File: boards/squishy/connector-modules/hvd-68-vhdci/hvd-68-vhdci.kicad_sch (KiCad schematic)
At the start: 14 parts, among them J1 SCSI PHY Mezz, J3 Conn_01x04, J4 VHDCI, U1 M24C02-RMC

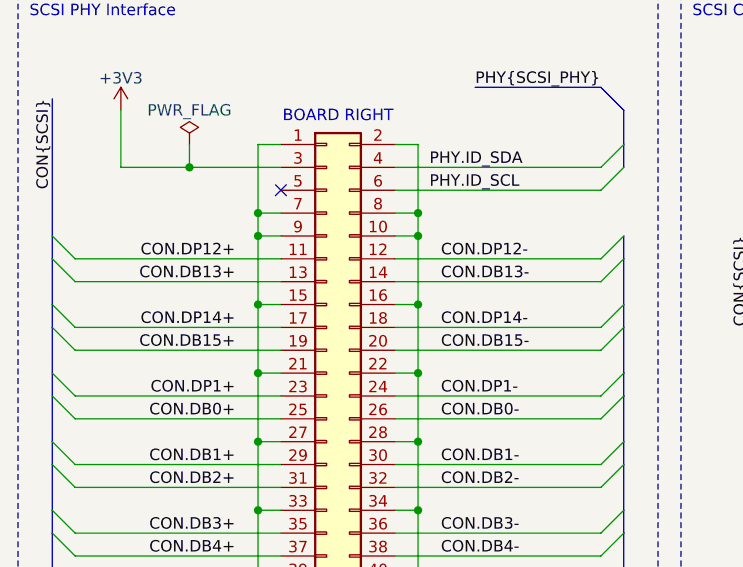
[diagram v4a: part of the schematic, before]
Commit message: squishy: connectors: s/DP12/DB12/g s/DP14/DB14/g
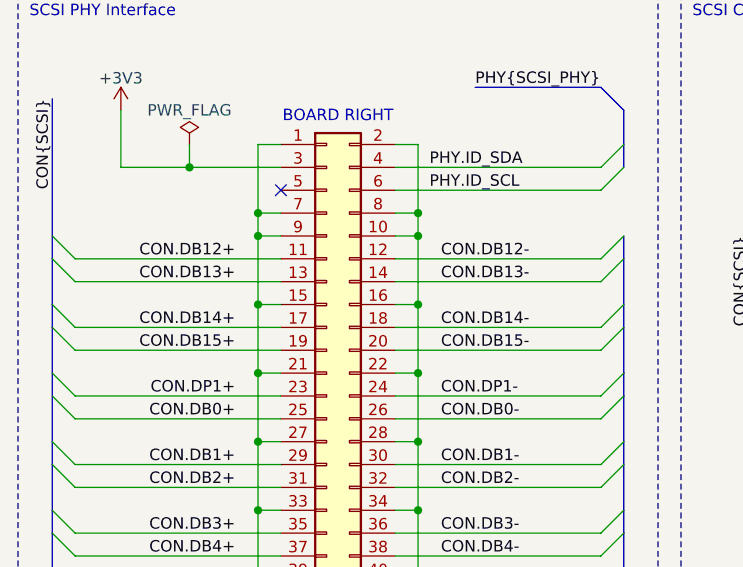
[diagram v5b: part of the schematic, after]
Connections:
- net CON.DP12+ is gone; now on net CON.DB12+: J1.11 (Pin_11)
- net CON.DP12- is gone; now on net CON.DB12-: J1.12 (Pin_12)
- net CON.DP14+ is gone; now on net CON.DB14+: J1.17 (Pin_17)
- net CON.DP14- is gone; now on net CON.DB14-: J1.18 (Pin_18)
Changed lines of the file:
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@@
 		)
 	)
-	(label "CON.DP14-"
+	(label "CON.DB14-"
 		(at 60.96 52.07 0)
 		(fields_autoplaced yes)
@@
 		)
 	)
-	(label "CON.DP12+"
+	(label "CON.DB12+"
 		(at 38.1 44.45 180)
 		(fields_autoplaced yes)
@@
 		)
 	)
-	(label "CON.DP12-"
+	(label "CON.DB12-"
 		(at 60.96 44.45 0)
 		(fields_autoplaced yes)
@@
 		)
 	)
-	(label "CON.DP14+"
+	(label "CON.DB14+"
 		(at 38.1 52.07 180)
 		(fields_autoplaced yes)

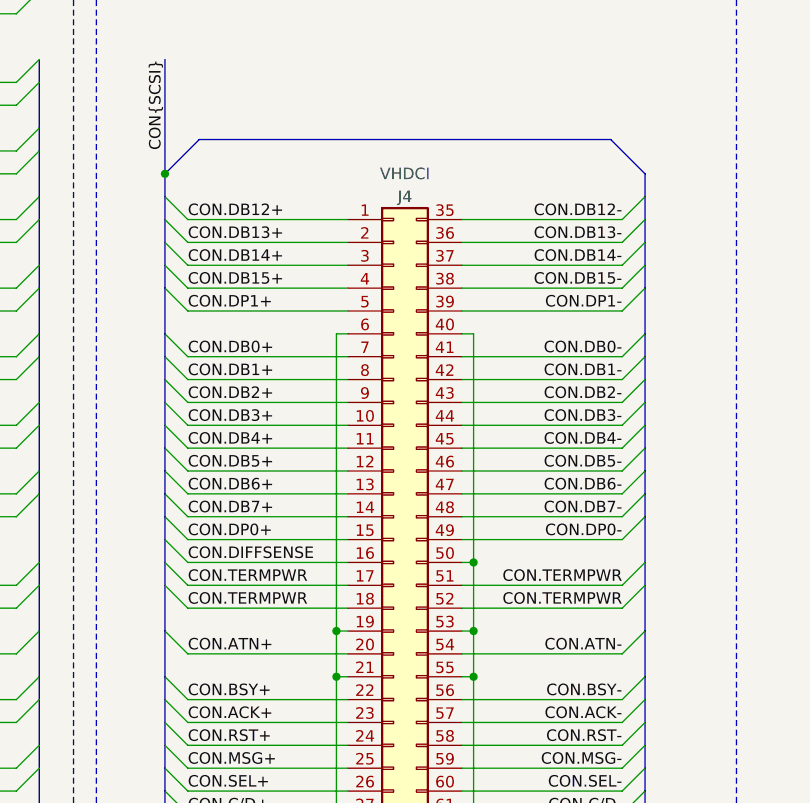
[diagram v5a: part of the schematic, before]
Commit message: squishy: connectors: updated SCSI connector metadata for hvd-68-vhdci
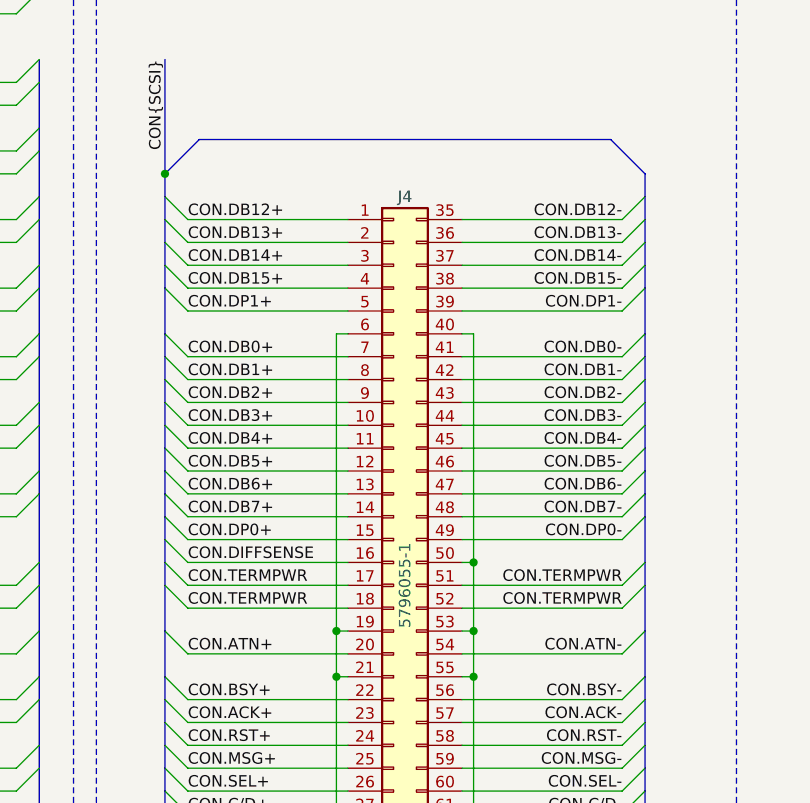
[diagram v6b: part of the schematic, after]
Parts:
- J4: value VHDCI -> 5796055-1; MFR (none) -> TE Connectivity; MPN (none) -> 5796055-1; URL (none) -> https://www.te.com/en/product-5796055-1.html
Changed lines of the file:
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@@
 			)
 		)
-		(property "Value" "VHDCI"
-			(at 121.92 54.61 0)
+		(property "Value" "5796055-1"
+			(at 121.92 100.33 90)
 			(effects
 				(font
@@
 			)
 		)
-		(property "Datasheet" "~"
+		(property "Datasheet" "https://www.te.com/commerce/DocumentDelivery/DDEController?Action=showdoc&DocId=Specification+Or+Standard%7F114-6057%7FD%7Fpdf%7FEnglish%7FENG_SS_114-6057_D.pdf%7F5796055-1"
 			(at 120.65 107.95 0)
 			(effects
@@
 			)
 		)
-		(property "Description" "Generic connector, double row, 02x34 counter clockwise pin numbering scheme (similar to DIP package numbering), with shielding"
+		(property "Description" "CHAMP 0.8mm Right Angle 68-pin VHDCI Connector"
 			(at 121.92 100.076 0)
 			(effects
 				(font
+					(size 1.27 1.27)
+				)
+				(hide yes)
+			)
+		)
+		(property "MFR" "TE Connectivity"
+			(at 121.92 100.33 0)
+			(effects
+				(font
+					(size 1.27 1.27)
+				)
+				(hide yes)
+			)
+		)
+		(property "MPN" "5796055-1"
+			(at 121.92 100.33 0)
+			(effects
+				(font
+					(size 1.27 1.27)
+				)
+				(hide yes)
+			)
+		)
+		(property "URL" "https://www.te.com/en/product-5796055-1.html"
+			(at 121.92 100.33 0)
+			(effects
+				(font

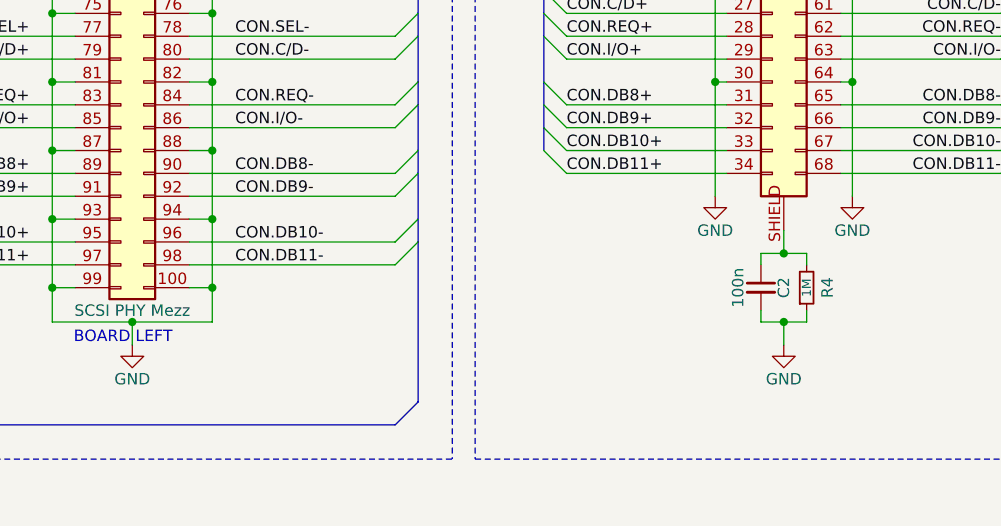
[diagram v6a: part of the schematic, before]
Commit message: squishy: connectors: cleaned up ERC on the hd-68-vhdci connector
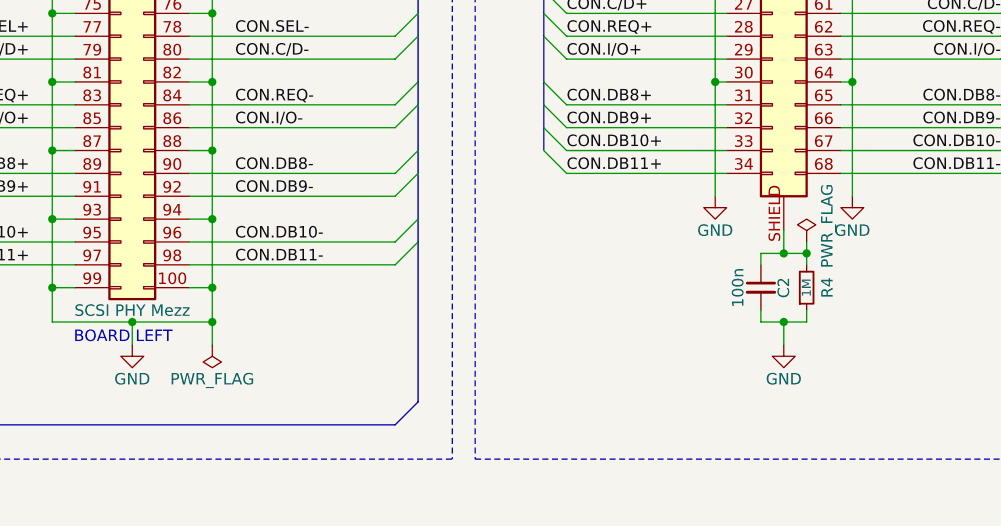
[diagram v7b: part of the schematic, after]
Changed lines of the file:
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@@
 	)
 	(junction
+		(at 124.46 152.4)
+		(diameter 0)
+		(color 0 0 0 0)
+	)
+	(junction
 		(at 58.42 125.73)
 		(diameter 0)
@@
 	)
 	(junction
+		(at 58.42 160.02)
+		(diameter 0)
+		(color 0 0 0 0)
+	)
+	(junction
 		(at 238.76 156.21)
 		(diameter 0)
@@
 	(wire
 		(pts
+			(xy 58.42 160.02) (xy 58.42 162.56)
+		)
+		(stroke
+			(width 0)
+			(type default)
+		)
+	)
+	(wire
+		(pts
 			(xy 78.74 67.31) (xy 55.88 67.31)
 		)
@@
 	(wire
 		(pts
+			(xy 124.46 151.13) (xy 124.46 152.4)
+		)
+		(stroke
+			(width 0)
+			(type default)
+		)
+	)
+	(wire
+		(pts
 			(xy 97.79 123.19) (xy 115.57 123.19)
 		)
@@
 	(symbol
 		(lib_id "power:PWR_FLAG")
+		(at 124.46 151.13 0)
+		(unit 1)
+		(exclude_from_sim no)
+		(in_bom yes)
+		(on_board yes)
+		(dnp no)
+		(property "Reference" "#FLG03"
+			(at 124.46 149.225 0)
+			(effects
+				(font
+					(size 1.27 1.27)
+				)
+				(hide yes)
+			)
+		)
+		(property "Value" "PWR_FLAG"
+			(at 126.746 149.352 90)
+			(effects
+				(font
+					(size 1.27 1.27)
+				)
+			)
+		)
+		(property "Footprint" ""
+			(at 124.46 151.13 0)
+			(effects
+				(font
+					(size 1.27 1.27)
+				)
+				(hide yes)
+			)
+		)
+		(property "Datasheet" "~"
+			(at 124.46 151.13 0)
+			(effects
+				(font
+					(size 1.27 1.27)
+				)
+				(hide yes)
+			)
+		)
+		(property "Description" "Special symbol for telling ERC where power comes from"
+			(at 124.46 151.13 0)
+			(effects
+				(font
+					(size 1.27 1.27)
+				)
+				(hide yes)
+			)
+		)
+		(pin "1"
+		)
+		(instances
+			(project "hvd-68-vhdci"
+				(path "/bd9eafec-5355-49e4-b2e3-916daacb0a86"
+					(reference "#FLG03")
+					(unit 1)
+				)
+			)
+		)
+	)
+	(symbol
+		(lib_id "power:PWR_FLAG")
 		(at 33.02 31.75 0)
 		(unit 1)
@@
 					(unit 1)
 				)
+			)
+		)
+	)
+	(symbol
+		(lib_id "power:PWR_FLAG")
+		(at 58.42 162.56 180)
+		(unit 1)
+		(exclude_from_sim no)
+		(in_bom yes)
+		(on_board yes)
+		(dnp no)
+		(property "Reference" "#FLG02"
+			(at 58.42 164.465 0)
+			(effects
+				(font
+					(size 1.27 1.27)
+				)
+				(hide yes)
+			)
+		)
+		(property "Value" "PWR_FLAG"
+			(at 58.42 166.37 0)
+			(effects
+				(font
+					(size 1.27 1.27)
+				)
+			)
+		)
+		(property "Footprint" ""
+			(at 58.42 162.56 0)
+			(effects
+				(font
+					(size 1.27 1.27)
+				)
+				(hide yes)
+			)
+		)
+		(property "Datasheet" "~"
+			(at 58.42 162.56 0)
+			(effects
+				(font
+					(size 1.27 1.27)
+				)
+				(hide yes)
+			)
+		)
+		(property "Description" "Special symbol for telling ERC where power comes from"
+			(at 58.42 162.56 0)
+			(effects
+				(font
+					(size 1.27 1.27)
+				)
+				(hide yes)
+			)
+		)
+		(pin "1"
+		)
+		(instances
+			(project "hvd-68-vhdci"
+				(path "/bd9eafec-5355-49e4-b2e3-916daacb0a86"
+					(reference "#FLG02")
+					(unit 1)
+				)

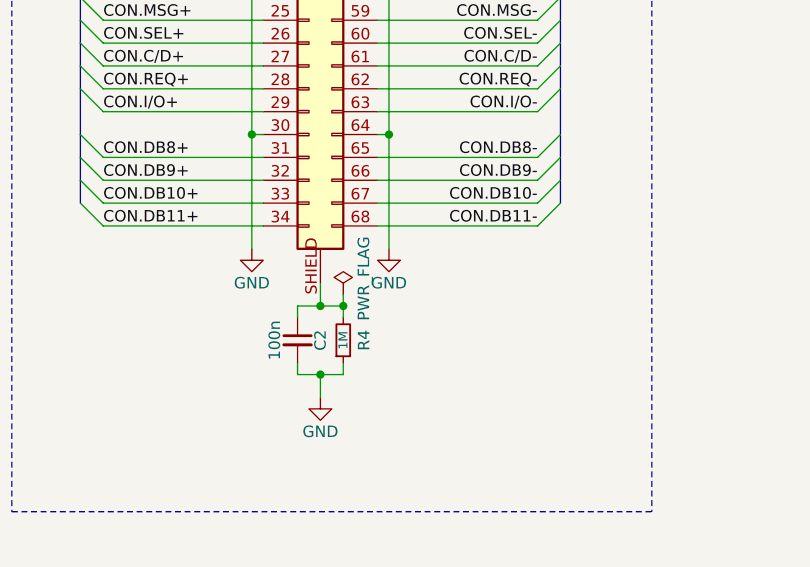
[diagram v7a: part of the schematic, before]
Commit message: squishy: connectors: Routed all and length matched half of the hvd-68-vhdci connector interface
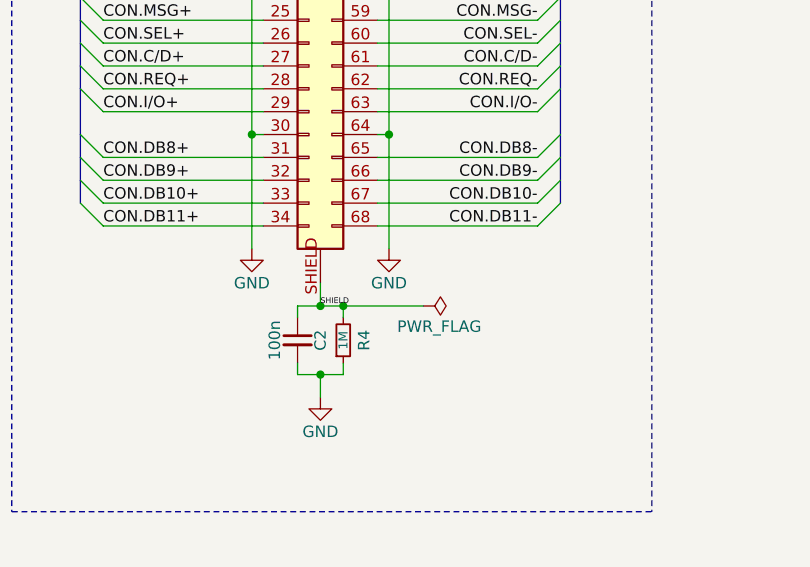
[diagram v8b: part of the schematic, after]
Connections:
- net SHIELD: now reaches C2.1, J4.SHIELD, R4.2
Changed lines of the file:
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@@
 	)
 	(junction
-		(at 124.46 152.4)
+		(at 58.42 125.73)
 		(diameter 0)
 		(color 0 0 0 0)
 	)
 	(junction
-		(at 58.42 125.73)
+		(at 40.64 64.77)
 		(diameter 0)
 		(color 0 0 0 0)
 	)
 	(junction
-		(at 40.64 64.77)
+		(at 124.46 152.4)
 		(diameter 0)
 		(color 0 0 0 0)
@@
 	(wire
 		(pts
+			(xy 124.46 152.4) (xy 133.35 152.4)
+		)
+		(stroke
+			(width 0)
+			(type default)
+		)
+	)
+	(wire
+		(pts
 			(xy 114.3 133.35) (xy 114.3 146.05)
 		)
@@
 	(wire
 		(pts
-			(xy 124.46 151.13) (xy 124.46 152.4)
-		)
-		(stroke
-			(width 0)
-			(type default)
-		)
-	)
-	(wire
-		(pts
 			(xy 97.79 123.19) (xy 115.57 123.19)
 		)
@@
 		)
 	)
+	(label "SHIELD"
+		(at 121.92 152.4 0)
+		(fields_autoplaced yes)
+		(effects
+			(font
+				(size 0.635 0.635)
+			)
+			(justify left bottom)
+		)
+	)
 	(label "CON.DB0+"
 		(at 97.79 74.93 0)
@@
 	(symbol
 		(lib_id "power:PWR_FLAG")
-		(at 124.46 151.13 0)
+		(at 133.35 152.4 270)
 		(unit 1)
 		(exclude_from_sim no)
@@
 		(dnp no)
 		(property "Reference" "#FLG03"
-			(at 124.46 149.225 0)
+			(at 135.255 152.4 0)
 			(effects
 				(font
@@
 		)
 		(property "Value" "PWR_FLAG"
-			(at 126.746 149.352 90)
+			(at 135.128 154.686 90)
 			(effects
 				(font
@@
 		)
 		(property "Footprint" ""
-			(at 124.46 151.13 0)
+			(at 133.35 152.4 0)
 			(effects
 				(font
@@
 		)
 		(property "Datasheet" "~"
-			(at 124.46 151.13 0)
+			(at 133.35 152.4 0)
 			(effects
 				(font
@@
 		)
 		(property "Description" "Special symbol for telling ERC where power comes from"
-			(at 124.46 151.13 0)
+			(at 133.35 152.4 0)
 			(effects
 				(font
